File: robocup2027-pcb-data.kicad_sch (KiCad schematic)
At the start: 40 parts, among them M5 Motor_Servo, M6 Motor_Servo, Q1 BPW40, Q2 BPW40, U1 ESP32-DEVKITC-32E

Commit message: updating footprints
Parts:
- U1: footprint ESP32-DEVKITC-32E:MODULE_ESP32-DEVKITC-32E -> robo:MODULE_ESP32-DEVKITC-32E
- U12, U4: footprint (none) -> robo:AE-HX711
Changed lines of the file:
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@@
 			)
 		)
-		(property "Footprint" ""
+		(property "Footprint" "robo:AE-HX711"
 			(at 242.57 138.43 0)
 			(effects
@@
 			)
 		)
-		(property "Footprint" "ESP32-DEVKITC-32E:MODULE_ESP32-DEVKITC-32E"
+		(property "Footprint" "robo:MODULE_ESP32-DEVKITC-32E"
 			(at 114.3 146.05 0)
 			(effects
@@
 			)
 		)
-		(property "Footprint" ""
+		(property "Footprint" "robo:AE-HX711"
 			(at 242.57 100.33 0)
 			(effects

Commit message: assigning footprints
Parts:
- U11: footprint (none) -> robo:M78AR033
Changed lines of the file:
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@@
 			)
 		)
-		(property "Footprint" ""
+		(property "Footprint" "robo:M78AR033"
 			(at 101.6 36.83 0)
 			(effects

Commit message: assigned all footprints except the motors
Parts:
- U10, U5, U6, U7, U8, U9: footprint (none) -> robo:VL53L1X-ToF
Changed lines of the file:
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@@
 			)
 		)
-		(property "Footprint" ""
+		(property "Footprint" "robo:VL53L1X-ToF"
 			(at 203.2 78.74 0)
 			(effects
@@
 			)
 		)
-		(property "Footprint" ""
+		(property "Footprint" "robo:VL53L1X-ToF"
 			(at 203.2 40.64 0)
 			(effects
@@
 			)
 		)
-		(property "Footprint" ""
+		(property "Footprint" "robo:VL53L1X-ToF"
 			(at 203.2 59.69 0)
 			(effects
@@
 			)
 		)
-		(property "Footprint" ""
+		(property "Footprint" "robo:VL53L1X-ToF"
 			(at 203.2 116.84 0)
 			(effects
@@
 			)
 		)
-		(property "Footprint" ""
+		(property "Footprint" "robo:VL53L1X-ToF"
 			(at 203.2 97.79 0)
 			(effects
@@
 			)
 		)
-		(property "Footprint" ""
+		(property "Footprint" "robo:VL53L1X-ToF"
 			(at 203.2 135.89 0)
 			(effects

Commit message: end of the day
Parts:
- U2: footprint robo:DS-850K-S-ON -> robo:voltmeter
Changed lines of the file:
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@@
 			)
 		)
-		(property "Footprint" "robo:DS-850K-S-ON"
+		(property "Footprint" "robo:voltmeter"
 			(at 22.86 77.47 0)
 			(effects

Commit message: update
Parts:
- C2, C8: footprint robo:5.08mm_capacitor_1 -> robo:capacitor
- Q1, Q2: footprint LED_THT:LED_D5.0mm_Clear -> robo:2.54mm_capacitor
- U11: footprint robo:M78AR033 -> robo:DCDC-M78AR033-0.5
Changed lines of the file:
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@@
 			)
 		)
-		(property "Footprint" "robo:5.08mm_capacitor_1"
+		(property "Footprint" "robo:capacitor"
 			(at 87.3252 82.55 0)
 			(effects
@@
 			)
 		)
-		(property "Footprint" "LED_THT:LED_D5.0mm_Clear"
+		(property "Footprint" "robo:2.54mm_capacitor"
 			(at 247.904 47.752 0)
 			(effects
@@
 			)
 		)
-		(property "Footprint" "LED_THT:LED_D5.0mm_Clear"
+		(property "Footprint" "robo:2.54mm_capacitor"
 			(at 247.904 64.262 0)
 			(effects
@@
 			)
 		)
-		(property "Footprint" "robo:5.08mm_capacitor_1"
+		(property "Footprint" "robo:capacitor"
 			(at 92.4052 36.83 0)
 			(effects
@@
 			)
 		)
-		(property "Footprint" "robo:M78AR033"
+		(property "Footprint" "robo:DCDC-M78AR033-0.5"
 			(at 101.6 36.83 0)
 			(effects

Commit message: done with the schematics
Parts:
- added C9: 0.1uF, robo:2.54mm_capacitor, symbol Device:C
- added M7, M8: ~, symbol robo:STS3032
- added U13: ~, symbol robo:fe-urt-2
- added U15: ~, symbol robo:Tof-VL53L0X
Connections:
- net MOTOR_2 is gone; now on net STS3032_signal: M2.3 (Signal)
- net MOTOR_3 is gone; now on net STS3032_signal: M3.3 (Signal)
- net MOTOR_4 is gone; now on net STS3032_signal: M4.3 (Signal)
- net +5V: now also U13.3 (Sig)
- net +6V: now also M7.2 (VCC), M8.2 (VCC)
- net GND: now also C9.2, M7.1 (GND), M8.1 (GND), U13.4 (GND), U15.2 (GND)
- net I2C_SCL: now also U15.4 (SCL)
- net I2C_SDA: now also U15.3 (SDA)
- net FE-URT-2-TXD: now reaches U1.J3_11 (IO17)
- net FE-URT-2-TXD: now also U13.1 (TXD)
- net FE-URT-2-RXD: now reaches U1.J3_12 (IO16)
- net FE-URT-2-RXD: now also U13.2 (RXD)
- net MOTOR_1 renamed STS3032_signal
- net STS3032_signal: now also M7.3 (Signal), M8.3 (Signal), U13.3 (Sig)
- new net: C9.1, U15.1 (V+)
- no-connect marks 48 -> 51
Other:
- note added: "FE-URT-2"

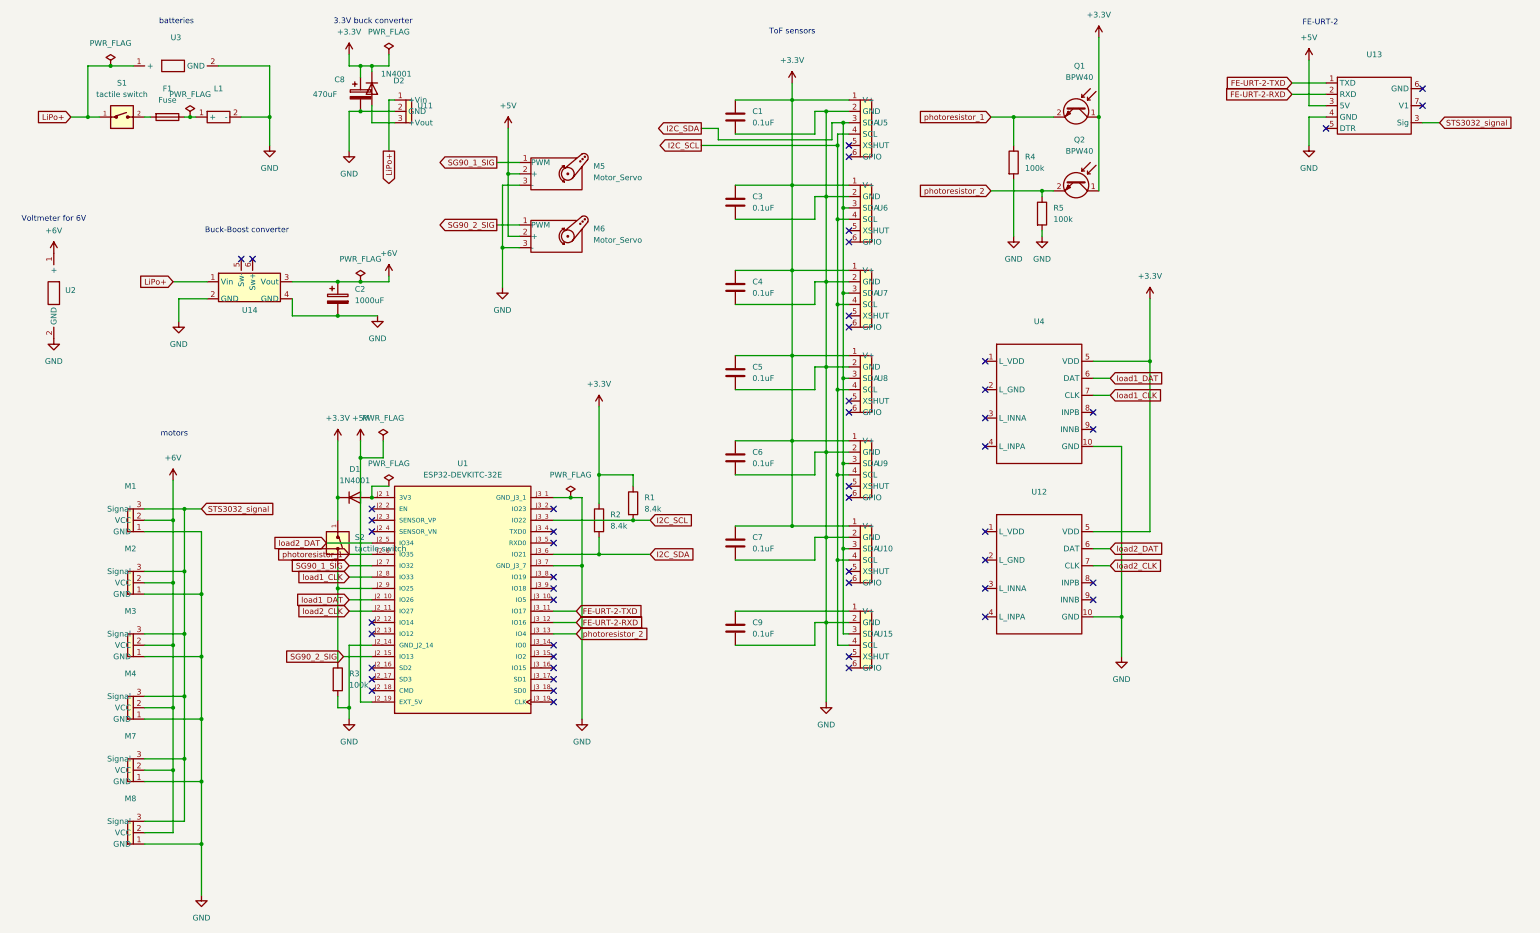
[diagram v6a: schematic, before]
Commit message: assigned footprint
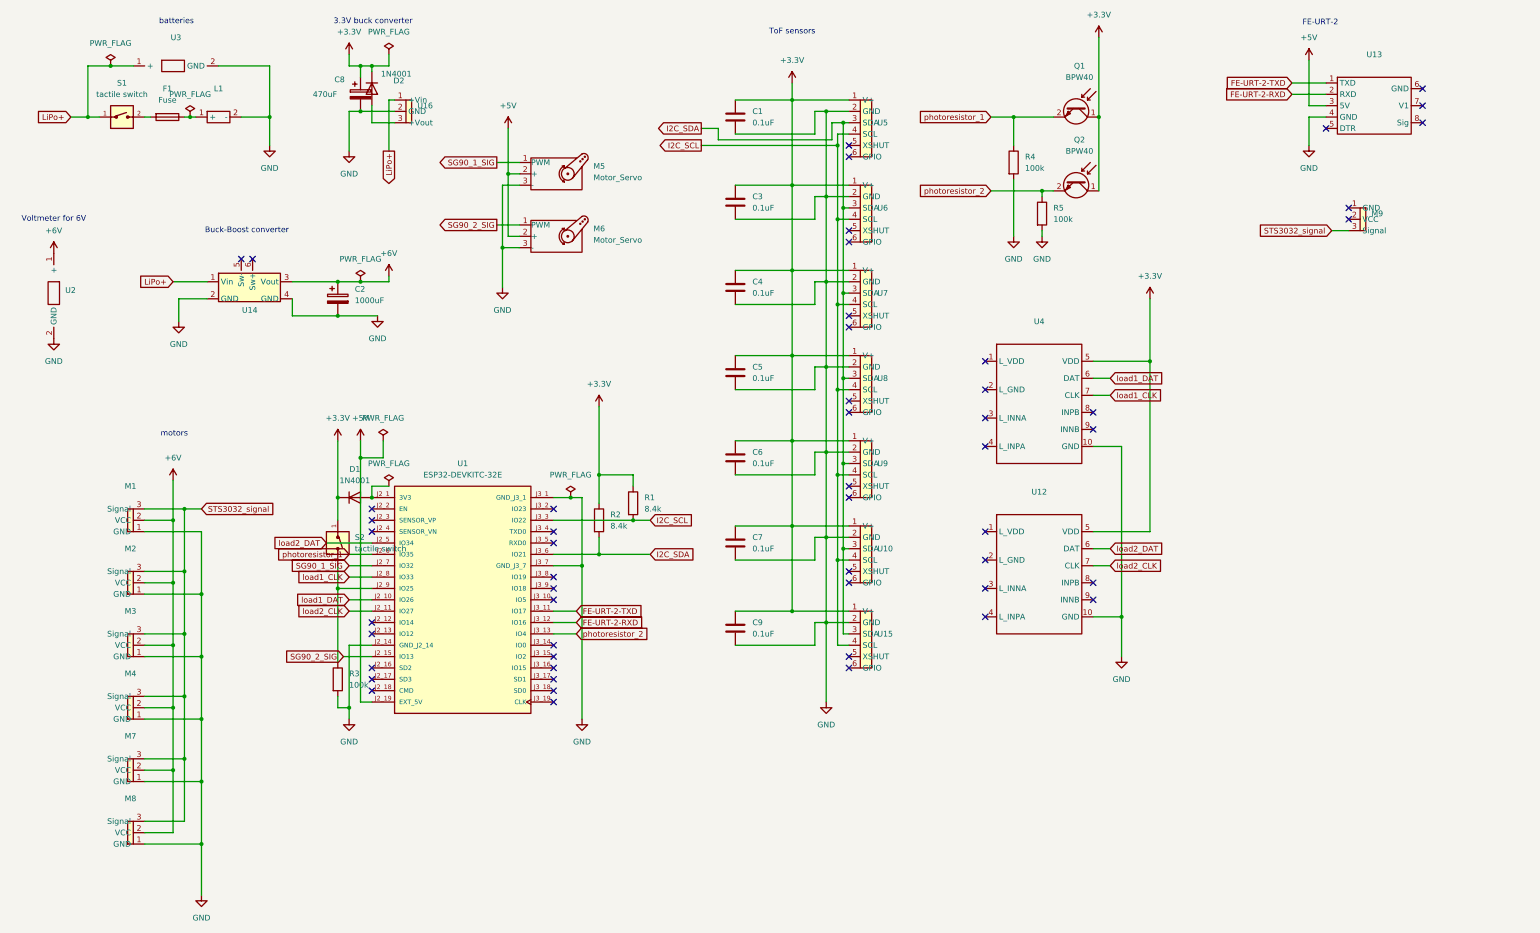
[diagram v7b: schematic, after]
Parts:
- removed U11: ~, robo:DCDC-M78AR033-0.5, symbol robo:DCDC-3.3v
- added M9: ~, robo:sts3032, symbol robo:STS3032
- added U16: ~, robo:DCDC-M78AR033-0.5, symbol robo:DCDC-3.3v
- M1, M2, M3, M4, M7, M8: footprint (none) -> robo:sts3032
- U13: footprint (none) -> robo:fe-urt-2
- U15: footprint (none) -> robo:VL53L1X-ToF
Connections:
- net +3.3V: now also C9.1, U15.1 (V+)
- net GND: now also U16.2 (GND)
- net LiPo+: now also U16.1 (+Vin)
- net STS3032_signal: now also M9.3 (Signal); no longer U13.3 (Sig)
- net at D2.2 (A): now also U16.3 (+Vout)
- no-connect marks 51 -> 54
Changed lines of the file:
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@@
 	)
 	(junction
+		(at 187.96 148.59)
+		(diameter 0)
+		(color 0 0 0 0)
+	)
+	(junction
 		(at 86.36 143.51)
 		(diameter 0)
@@
 	)
 	(no_connect
+		(at 312.42 58.42)
+	)
+	(no_connect
 		(at 231.14 99.06)
 	)
@@
 	)
 	(no_connect
+		(at 328.93 39.37)
+	)
+	(no_connect
+		(at 312.42 60.96)
+	)
+	(no_connect
 		(at 255.27 142.24)
 	)
@@
 	(wire
 		(pts
+			(xy 308.61 63.5) (xy 312.42 63.5)
+		)
+		(stroke
+			(width 0)
+			(type default)
+		)
+	)
+	(wire
+		(pts
 			(xy 134.62 135.89) (xy 144.78 135.89)
 		)
@@
 	(wire
 		(pts
-			(xy 328.93 39.37) (xy 332.74 39.37)
-		)
-		(stroke
-			(width 0)
-			(type default)
-		)
-	)
-	(wire
-		(pts
 			(xy 35.56 26.67) (xy 30.48 26.67)
 		)
@@
 	(wire
 		(pts
-			(xy 175.26 148.59) (xy 200.66 148.59)
+			(xy 175.26 148.59) (xy 187.96 148.59)
 		)
 		(stroke
@@
 	(wire
 		(pts
+			(xy 187.96 148.59) (xy 200.66 148.59)
+		)
+		(stroke
+			(width 0)
+			(type default)
+		)
+	)
+	(wire
+		(pts
 			(xy 55.88 130.81) (xy 55.88 144.78)
 		)
@@
 	(wire
 		(pts
+			(xy 187.96 129.54) (xy 187.96 148.59)
+		)
+		(stroke
+			(width 0)
+			(type default)
+		)
+	)
+	(wire
+		(pts
 			(xy 199.39 39.37) (xy 196.85 39.37)
 		)
@@
 	(global_label "STS3032_signal"
 		(shape input)
-		(at 332.74 39.37 0)
+		(at 308.61 63.5 180)
 		(fields_autoplaced yes)
 		(effects
@@
 				(size 1.27 1.27)
 			)
-			(justify left)
+			(justify right)
 		)
 		(property "Intersheetrefs" "${INTERSHEET_REFS}"
-			(at 350.6625 39.37 0)
+			(at 290.6875 63.5 0)
 			(effects
 				(font
 					(size 1.27 1.27)
 				)
-				(justify left)
+				(justify right)
 				(hide yes)
 			)
@@
 			)
 		)
-		(property "Footprint" ""
+		(property "Footprint" "robo:sts3032"
 			(at 40.005 142.24 0)
 			(effects
@@
 			)
 		)
-		(property "Footprint" ""
+		(property "Footprint" "robo:sts3032"
 			(at 40.005 184.15 0)
 			(effects
@@
 	)
 	(symbol
-		(lib_id "robo:fe-urt-2")
-		(at 314.96 35.56 0)
-		(unit 1)
-		(exclude_from_sim no)
-		(in_bom yes)
-		(on_board yes)
-		(dnp no)
-		(fields_autoplaced yes)
-		(property "Reference" "U13"
-			(at 318.135 24.13 0)
-			(effects
-				(font
-					(size 1.27 1.27)
-				)
-			)
-		)
-		(property "Value" "~"
-			(at 318.135 26.67 0)
-			(effects
-				(font
-					(size 1.27 1.27)
-				)
-			)
-		)
-		(property "Footprint" ""
-			(at 314.96 35.56 0)
-			(effects
-				(font
-					(size 1.27 1.27)
-				)
-				(hide yes)
-			)
-		)
-		(property "Datasheet" ""
-			(at 314.96 35.56 0)
-			(effects
-				(font
-					(size 1.27 1.27)
-				)
-				(hide yes)
-			)
-		)
-		(property "Description" ""
-			(at 314.96 35.56 0)
-			(effects
-				(font
-					(size 1.27 1.27)
-				)
-				(hide yes)
-			)
-		)
-		(pin "6"
-		)
-		(pin "7"
-		)
-		(pin "3"
-		)
-		(pin "2"
-		)
-		(pin "1"
-		)
-		(pin "5"
-		)
-		(pin "4"
-		)
-		(pin "3"
-		)
-		(instances
-			(project "robocup2027-pcb-data"
-				(path "/fda8bdee-4e79-4e78-9174-7c0702f316a4"
-					(reference "U13")
-					(unit 1)
-				)
-			)
-		)
-	)
-	(symbol
 		(lib_id "power:+5V")
 		(at 303.53 25.4 0)
@@
 			)
 		)
-		(property "Footprint" ""
+		(property "Footprint" "robo:sts3032"
 			(at 40.005 170.18 0)
 			(effects
@@
 			)
 		)
-		(property "Footprint" ""
+		(property "Footprint" "robo:VL53L1X-ToF"
 			(at 203.2 154.94 0)
 			(effects
@@
 	)
 	(symbol
+		(lib_id "robo:STS3032")
+		(at 314.96 60.96 270)
+		(unit 1)
+		(exclude_from_sim no)
+		(in_bom yes)
+		(on_board yes)
+		(dnp no)
+		(fields_autoplaced yes)
+		(property "Reference" "M9"
+			(at 317.5 59.6899 90)
+			(effects
+				(font
+					(size 1.27 1.27)
+				)
+				(justify left)
+			)
+		)
+		(property "Value" "~"
+			(at 317.5 62.2299 90)
+			(effects
+				(font
+					(size 1.27 1.27)
+				)
+				(justify left)
+			)
+		)
+		(property "Footprint" "robo:sts3032"
+			(at 315.595 60.96 0)
+			(effects
+				(font
+					(size 1.27 1.27)
+				)
+				(hide yes)
+			)
+		)
+		(property "Datasheet" ""
+			(at 315.595 60.96 0)
+			(effects
+				(font
+					(size 1.27 1.27)
+				)
+				(hide yes)
+			)
+		)
+		(property "Description" ""
+			(at 315.595 60.96 0)
+			(effects
+				(font
+					(size 1.27 1.27)
+				)
+				(hide yes)
+			)
+		)
+		(pin "3"
+		)
+		(pin "2"
+		)
+		(pin "1"
+		)
+		(instances
+			(project "robocup2027-pcb-data"
+				(path "/fda8bdee-4e79-4e78-9174-7c0702f316a4"
+					(reference "M9")
+					(unit 1)
+				)
+			)
+		)
+	)
+	(symbol
 		(lib_id "robo:Tof-VL53L0X")
 		(at 201.93 40.64 270)
@@
 			)
 		)
-		(property "Footprint" ""
+		(property "Footprint" "robo:sts3032"
 			(at 40.005 156.21 0)
 			(effects
@@
 			)
 		)
-		(property "Footprint" ""
+		(property "Footprint" "robo:sts3032"
 			(at 40.005 198.12 0)
 			(effects
@@
 			)
 		)
-		(property "Footprint" ""
+		(property "Footprint" "robo:sts3032"
 			(at 40.005 128.27 0)
 			(effects
@@
 	)
 	(symbol
-		(lib_id "robo:DCDC-3.3v")
-		(at 101.6 36.83 270)
+		(lib_id "robo:fe-urt-2")
+		(at 314.96 35.56 0)
 		(unit 1)
 		(exclude_from_sim no)
@@
 		(dnp no)
 		(fields_autoplaced yes)
-		(property "Reference" "U11"
-			(at 104.14 35.5599 90)
+		(property "Reference" "U13"
+			(at 318.135 24.13 0)
 			(effects
 				(font
 					(size 1.27 1.27)
 				)
-				(justify left)
 			)
 		)
 		(property "Value" "~"
-			(at 104.14 38.0999 90)
+			(at 318.135 26.67 0)
 			(effects
 				(font
 					(size 1.27 1.27)
 				)
-				(justify left)
 			)
 		)
-		(property "Footprint" "robo:DCDC-M78AR033-0.5"
-			(at 101.6 36.83 0)
+		(property "Footprint" "robo:fe-urt-2"
+			(at 314.96 35.56 0)
 			(effects
 				(font
@@
 		)
 		(property "Datasheet" ""
-			(at 101.6 36.83 0)
+			(at 314.96 35.56 0)
 			(effects
 				(font
@@
 		)
 		(property "Description" ""
-			(at 101.6 36.83 0)
+			(at 314.96 35.56 0)
 			(effects
 				(font
@@
 			)
 		)
-		(pin "1"
+		(pin "8"
 		)
-		(pin "3"
+		(pin "5"
+		)
+		(pin "6"
 		)
 		(pin "2"
 		)
+		(pin "1"
+		)
+		(pin "7"
+		)
+		(pin "4"
+		)
+		(pin "3"
+		)
 		(instances
 			(project "robocup2027-pcb-data"
 				(path "/fda8bdee-4e79-4e78-9174-7c0702f316a4"
-					(reference "U11")
+					(reference "U13")
 					(unit 1)
 				)
@@
 					(unit 1)
 				)
+			)
+		)
+	)
+	(symbol
+		(lib_name "DCDC-3.3v_1")
+		(lib_id "robo:DCDC-3.3v")
+		(at 101.6 36.83 270)
+		(unit 1)
+		(exclude_from_sim no)
+		(in_bom yes)
+		(on_board yes)
+		(dnp no)
+		(fields_autoplaced yes)
+		(property "Reference" "U16"
+			(at 104.14 35.5599 90)
+			(effects
+				(font
+					(size 1.27 1.27)
+				)
+				(justify left)
+			)
+		)
+		(property "Value" "~"
+			(at 104.14 38.0999 90)
+			(effects
+				(font
+					(size 1.27 1.27)
+				)
+				(justify left)
+			)
+		)
+		(property "Footprint" "robo:DCDC-M78AR033-0.5"
+			(at 101.6 36.83 0)
+			(effects
+				(font
+					(size 1.27 1.27)
+				)
+				(hide yes)
+			)
+		)
+		(property "Datasheet" ""
+			(at 101.6 36.83 0)
+			(effects
+				(font
+					(size 1.27 1.27)
+				)
+				(hide yes)
+			)
+		)
+		(property "Description" ""
+			(at 101.6 36.83 0)
+			(effects
+				(font
+					(size 1.27 1.27)
+				)
+				(hide yes)
+			)
+		)
+		(pin "3"
+		)
+		(pin "1"
+		)
+		(pin "2"
+		)
+		(instances
+			(project "robocup2027-pcb-data"
+				(path "/fda8bdee-4e79-4e78-9174-7c0702f316a4"
+					(reference "U16")
+					(unit 1)
+				)
